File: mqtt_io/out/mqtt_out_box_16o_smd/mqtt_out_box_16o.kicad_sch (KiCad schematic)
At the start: 105 parts, among them J1 Conn_01x04_Pin, K1 FINDER-40.31, K10 FINDER-40.31, K11 FINDER-40.31, K12 FINDER-40.31, K13 FINDER-40.31, K14 FINDER-40.31, K15 FINDER-40.31, K16 FINDER-40.31, K2 FINDER-40.31, K3 FINDER-40.31, K4 FINDER-40.31, K5 FINDER-40.31, K6 FINDER-40.31, K7 FINDER-40.31, K8 FINDER-40.31, K9 FINDER-40.31, Q1 IRLML0030, Q10 IRLML0030, Q11 IRLML0030, Q12 IRLML0030, Q13 IRLML0030, Q14 IRLML0030, Q15 IRLML0030, Q16 IRLML0030, Q2 IRLML0030, Q3 IRLML0030, Q4 IRLML0030, Q5 IRLML0030, Q6 IRLML0030, Q7 IRLML0030, Q8 IRLML0030, Q9 IRLML0030, U1 MCP23017_SO

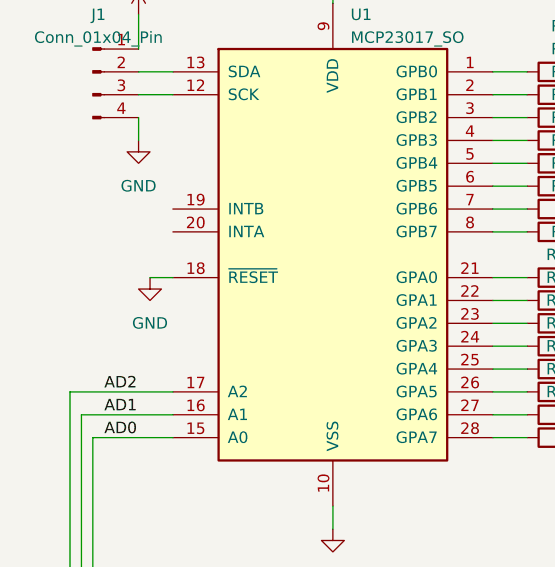
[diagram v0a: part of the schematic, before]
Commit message: neue Dateien eingefügt.
out Platine rev 2, testprogramm für pi pico
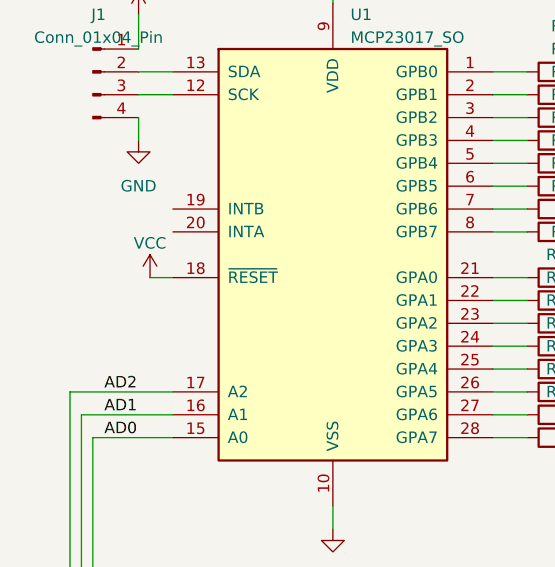
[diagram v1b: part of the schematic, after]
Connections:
- net GND: no longer U1.18 (~{RESET})
- net VCC: now also U1.18 (~{RESET})
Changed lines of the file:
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@@
     (stroke (width 0) (type default))
   )
+  (wire (pts (xy 25.4 49.53) (xy 27.94 49.53))
+    (stroke (width 0) (type default))
+  )
   (wire (pts (xy 269.24 77.47) (xy 275.59 77.47))
     (stroke (width 0) (type default))
@@
     (stroke (width 0) (type default))
   )
-  (wire (pts (xy 25.4 49.53) (xy 27.94 49.53))
-    (stroke (width 0) (type default))
-  )
   (wire (pts (xy 236.22 105.41) (xy 236.22 125.73))
     (stroke (width 0) (type default))
@@
     )
   )
-  (symbol (lib_id "power:GND") (at 25.4 49.53 0) (unit 1)
-    (in_bom yes) (on_board yes) (dnp no) (fields_autoplaced)
-    (property "Reference" "#PWR011" (at 25.4 55.88 0)
-      (effects (font (size 1.27 1.27)) hide)
-    )
-    (property "Value" "GND" (at 25.4 54.61 0)
-      (effects (font (size 1.27 1.27)))
-    )
-    (property "Footprint" "" (at 25.4 49.53 0)
-      (effects (font (size 1.27 1.27)) hide)
-    )
-    (property "Datasheet" "" (at 25.4 49.53 0)
-      (effects (font (size 1.27 1.27)) hide)
-    )
-    (pin "1")
-    (instances
-      (project "mqtt_out_box_16o"
-        (path "/c627dcd6-05c4-47a7-af36-f14e587162a0"
-          (reference "#PWR011") (unit 1)
-        )
-      )
-    )
-  )
   (symbol (lib_id "Device:R") (at 71.12 57.15 90) (unit 1)
     (in_bom yes) (on_board yes) (dnp no) (fields_autoplaced)
@@
       (effects (font (size 1.27 1.27)) hide)
     )
-    (pin "2")
     (pin "1")
+    (pin "2")
     (pin "3")
     (instances
@@
         )
       )
+    )
+  )
+  (symbol (lib_id "power:VCC") (at 25.4 49.53 0) (unit 1)
+    (in_bom yes) (on_board yes) (dnp no) (fields_autoplaced)
+    (property "Reference" "#PWR011" (at 25.4 53.34 0)
+      (effects (font (size 1.27 1.27)) hide)
+    )
+    (property "Value" "VCC" (at 25.4 45.72 0)
+      (effects (font (size 1.27 1.27)))
+    )
+    (property "Footprint" "" (at 25.4 49.53 0)
+      (effects (font (size 1.27 1.27)) hide)
+    )
+    (property "Datasheet" "" (at 25.4 49.53 0)
+      (effects (font (size 1.27 1.27)) hide)
+    )
+    (pin "1")
+    (instances
+      (project "mqtt_out_box_16o"
+        (path "/c627dcd6-05c4-47a7-af36-f14e587162a0"
+          (reference "#PWR011") (unit 1)
+        )
+      )
